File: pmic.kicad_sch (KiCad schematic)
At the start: 4 parts, among them U4 TPS6521907RHBR

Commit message: PMIC draft
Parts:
- added C25, C26, C27: GRM188R60J476ME15D, pepy_sym_lib:[CAP_SMD_0603_1608Metric], symbol pepy_sym_lib:[CAP_SMD_0603_1608Metric]Murata Electronics GRM188R60J476ME15D
- added C28, C29, C30, C31, C32, C33, C34, C35, C36: CC0402KRX5R6BB225, pepy_sym_lib:[CAP_SMD_0402_1005Metric], symbol pepy_sym_lib:[CAP_SMD_0402_1005Metric]YAGEO CC0402KRX5R6BB225
- added L3: FPA252012D-R33MT0, pepy_sym_lib:[P_IND_SMD_1008_2520Metric], symbol pepy_sym_lib:[P_IND_SMD_1008_2520Metric]cjiang (Changjiang Microelectronics Tec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
- added L4, L5: FTM252010CR47MCTA, pepy_sym_lib:[P_IND_SMD_1008_2520Metric], symbol pepy_sym_lib:[P_IND_SMD_1008_2520Metric]cjiang (Changjiang Microelectronics Tec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
- added R66, R67: 0402WGF0000TCE, pepy_sym_lib:[RES_SMD_0402_1005Metric], symbol pepy_sym_lib:[RES_SMD_0402_1005Metric]UNI-ROYAL(Uniroyal Elec) 0402WGF0000TCE
- added R68, R69, R70, R71, R72, R73: 0201WMF1002TEE, pepy_sym_lib:[RES_SMD_0201_0603Metric], symbol pepy_sym_lib:[RES_SMD_0201_0603Metric]UNI-ROYAL(Uniroyal Elec) 0201WMF1002TEE
- added TP10: VDDA_0V85, pepy_sym_lib:[TEST_POINT]TestPoint_Pad_D1.0mm, symbol pepy_sym_lib:[TEST_POINT]TestPoint
- added TP11: VDDA_1V8, 2, symbol pepy_sym_lib:[TEST_POINT]TestPoint
- added TP12: VDD_2V5, pepy_sym_lib:[TEST_POINT]TestPoint_Pad_D1.0mm, symbol pepy_sym_lib:[TEST_POINT]TestPoint
- added TP6: VDD_CORE, pepy_sym_lib:[TEST_POINT]TestPoint_Pad_D1.0mm, symbol pepy_sym_lib:[TEST_POINT]TestPoint
- added TP7: VDD_1V8, pepy_sym_lib:[TEST_POINT]TestPoint_Pad_D1.0mm, symbol pepy_sym_lib:[TEST_POINT]TestPoint
- added TP8: VDD_1V2, pepy_sym_lib:[TEST_POINT]TestPoint_Pad_D1.0mm, symbol pepy_sym_lib:[TEST_POINT]TestPoint
- added TP9: VDD_SD, pepy_sym_lib:[TEST_POINT]TestPoint_Pad_D1.0mm, symbol pepy_sym_lib:[TEST_POINT]TestPoint
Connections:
- net GND: now also C14.1, U4.15 (AGND), U4.33 (ThermalPad), C25.1, C26.1, C27.1, C28.2, C29.2, C30.2, C31.2, C32.2, C33.2, C34.2, C35.2, C36.2, R66.2, R70.1
- net VSYS_5V: now also U4.13 (VSYS), C32.1, R68.2
- net at U4.1 (FB_B1): now also R66.1, R67.1
- net I2C0_SCL: now reaches U4.10 (SCL)
- net EXTINTn: now reaches U4.11 (nINT)
- net EXTINTn: now also R72.1
- net SD_VOLT_SEL: now reaches U4.12 (VSEL_SD/VSEL_DDR)
- net SD_VOLT_SEL: now also R69.1, R70.2
- net at U4.14 (VDD1P8): now also C31.1
- net VDD_3V3_EN: now reaches U4.17 (GPO2)
- net MCU_PORz: now reaches U4.18 (nRSTOUT)
- net MCU_PORz: now also R73.1
- net VDDA_0V85: now reaches U4.19 (VLDO2)
- net VDDA_0V85: now also C34.1, TP10.1
- net at U4.2 (LX_B1_1): now also U4.3 (LX_B1_2), L3.2
- net VDD_1V8: now reaches U4.20 (PVIN_LDO2)
- net VDD_1V8: now also U4.32 (FB_B2), C26.2, C29.1, L4.1, TP7.1
- net VDDA_1V8: now reaches U4.21 (VLDO3)
- net VDDA_1V8: now also C35.1, TP11.1
- net VDD_3V3: now reaches U4.22 (PVIN_LDO34)
- net VDD_3V3: now also U4.6 (PVIN_LDO1), C28.1, C30.1, R69.2, R71.2, R72.2, R73.2
- net VDD_2V5: now reaches U4.23 (VLDO4)
- net VDD_2V5: now also C36.1, TP12.1
- net VDD_1V2: now reaches U4.24 (FB_B3)
- net VDD_1V2: now also C27.2, L5.1, TP8.1
- net PWR_BTN: now reaches U4.25 (EN/PB/VSENSE)
- net PWR_BTN: now also R68.1
- net at U4.27 (LX_B3): now also L5.2
- net RESETSTATz: now reaches U4.28 (MODE/RESET)
- net at U4.29 (LX_B2): now also L4.2
- net PMIC_LPM_EN0: now reaches U4.31 (MODE/STBY)
- net PMIC_LPM_EN0: now also R71.1
- net VDD_SD: now reaches U4.7 (VLDO1)
- net VDD_SD: now also C33.1, TP9.1
- net I2C0_SDA: now reaches U4.9 (SDA)
- new net VDD_CORE: C25.2, L3.1, R67.2, TP6.1
- no-connect marks 0 -> 2
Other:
- note added: "0.75V 3.5A"
- note added: "1.2V 2A"
- note added: "1.8V 0.4A"
- note added: "1.8V 2A"
- note added: "BUCK1_VSET [hexadecimal]: 0x06"
- note added: "BUCK2_VSET [hexadecimal]: 0x24"
- note added: "BUCK3_VSET [hexadecimal]: 0x18"
- note added: "Design: CSTB252012H-R33M ((1008[M:2520]), 6.9A, 330nH)"
- note added: "Design: CSTB252012H-R47M (1008[M:2520]), 5A, 470nH)"
- note added: "External 3V3 (and 1V8) DC gives the input power for the LDOs"
- note added: "External INT into SoC respective pin (pull-up to negated logic)"
- note added: "For any other purposes?"
- note added: "Internal Reference Voltage: For Internal Use Only. Bypass this pin to ground with a 2.2µF or greater ceramic capacitor."
- note added: "Main Domain warm reset status output"
- note added: "Power Input for BUCK1. Bypass this pin to ground with a 4.7μF or greater ceramic capacitor. Voltage on PVIN_B1_1 pin must not exceed voltage on VSYS pin."
- note added: "Since the power management is handled by the PMIC, it's reasonable to toggle it."
- note added: "The TPS65219 provides three step-down converters, four LDOs, three general-purpose I/Os and three multiFunction pins. The system can be supplied by a single cell Li-Ion battery, two primary cells or a regulated supply. The device is characterized across a -40°C to +105°C temperature range, which makes the PMIC an excellent choice for various industrial applications. The I2C interface provides com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"
- moved on the sheet: C19, U4

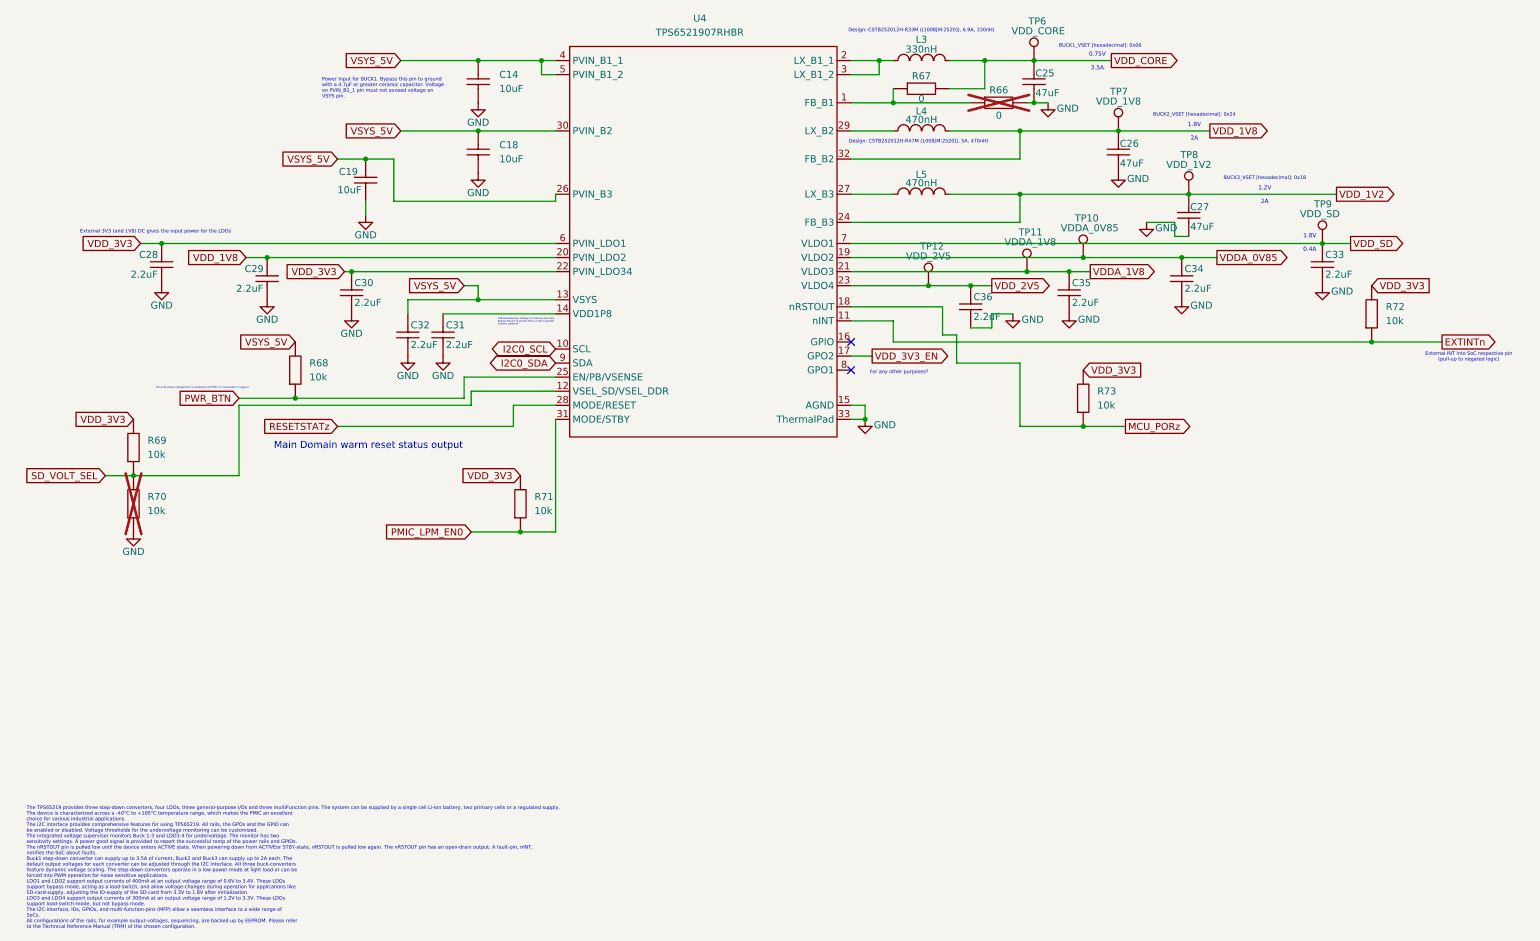
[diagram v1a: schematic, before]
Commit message: SD card changes
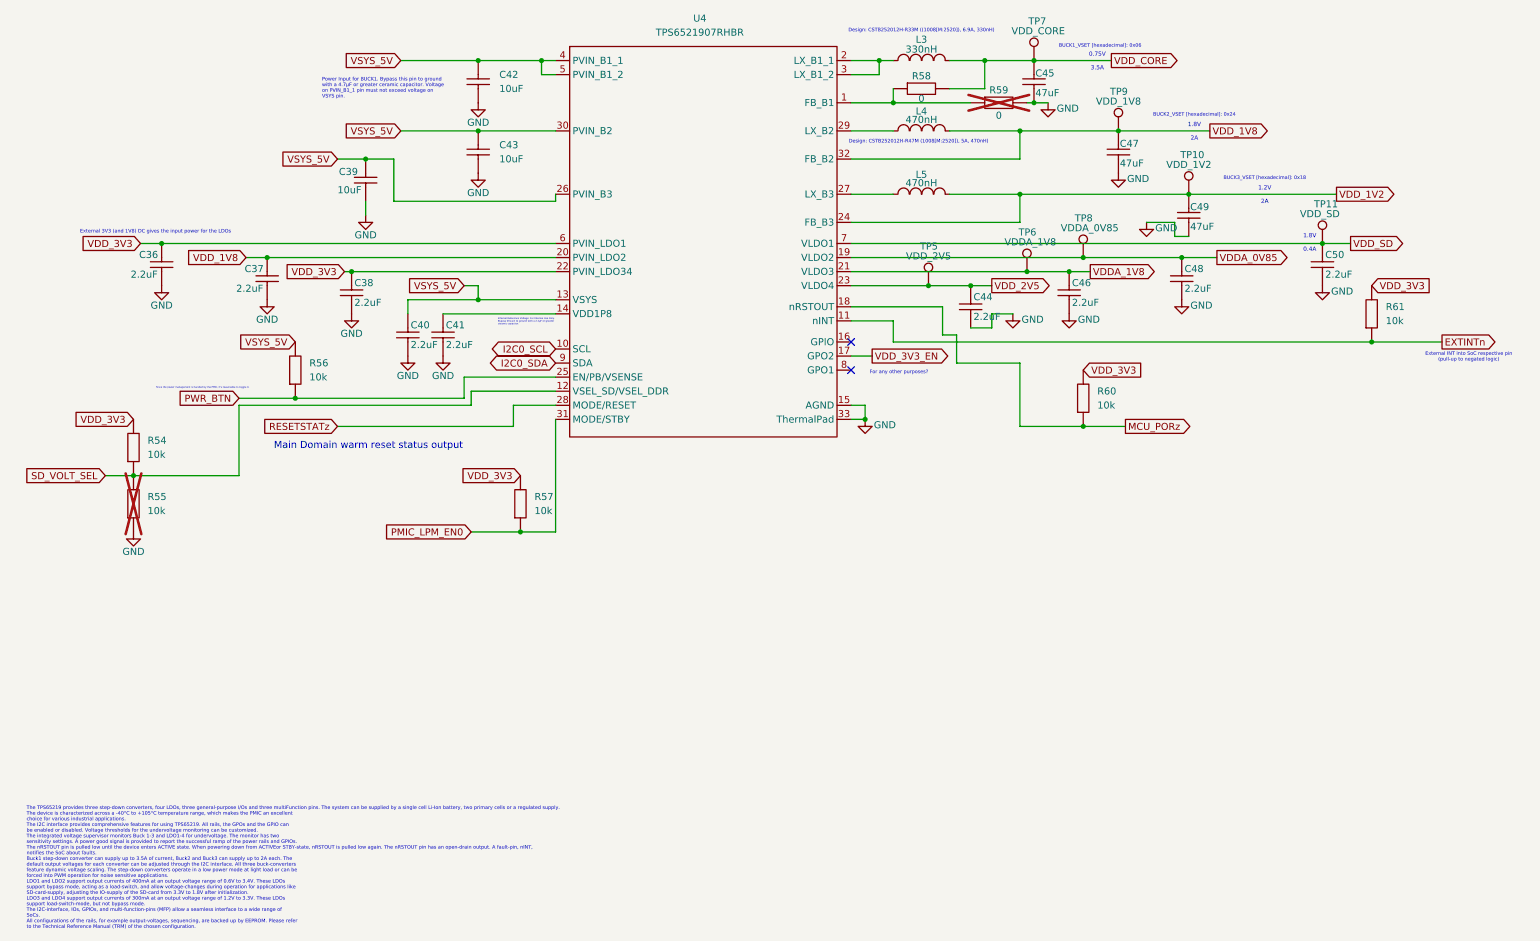
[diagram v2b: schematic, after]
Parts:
- renumbered C28 to C36, C29 to C37, C30 to C38, C19 to C39, C32 to C40, C31 to C41, C14 to C42, C18 to C43, C36 to C44, C25 to C45, C35 to C46, C26 to C47, C34 to C48, C27 to C49, C33 to C50, R69 to R54, R70 to R55, R68 to R56, R71 to R57, R67 to R58, R66 to R59, R73 to R60, R72 to R61, TP8 to TP10, TP9 to TP11, TP12 to TP5, TP11 to TP6, TP6 to TP7, TP10 to TP8, TP7 to TP9

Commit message: Bulk change
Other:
- note added: "1.8V/3.3V 0.4A"
- note removed: "1.8V 0.4A"
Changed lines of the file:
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@@
 		)
 	)
-	(text "1.8V\n\n0.4A"
+	(text "1.8V/3.3V\n\n\n0.4A"
 		(exclude_from_sim no)
-		(at 245.364 71.12 0)
+		(at 243.332 71.12 0)
 		(effects
 			(font
@@
 			"AAAAAIA/ZVUAAAAAAAAAAAAAAAAAAAAAAABwJetrqX8AAIhN+vhlVQAAAAAAAAAAAAAAAAAAAAAA"
 			"AIBN+vhlVQAAAAAAAAAAAAAAAAAAAAAAAJDMOe5lVQAACAAAAAAAAAAIAAAAAAAAAAIAAAAAAQAA"
-			"AAAAAAAAAAAAAAAAAAAAAMBhxvZlVQAACAAAAAAAAAAIAAAAAAAAAAAAAAAAAAAAAAAAAAAAAA=="
-		)
-	)
+			"AAAAAAAAAAAAAAAAAAAAAMBhxvZlVQAACAAAAAAAAAAIAAAAAAAAAAAAAAAAAAAAAAAAAAAAAAAA"
+			"AAAAAAAAAAAAAAAAAAAAAAAAAAAAAAAAAAAAAAAAAAAAAAAAAAAAAAAAAAAAAAAAAAAAAAAAAAAA"
+			"AAAAAAAAAAAAAAAAAAAAAAAAAAAAAAAAAAAAAAAAAAAAAAAAAAAAAAAAAAAAAAAAAAAAAAAAAAAA"
+			"AAAAAAAAAAAAAAAAAAAAAAAAAAAAAAAAAAAAAAAAAAAAAAAAAAAAAAAAAAAAAAAAAAAAAAAAAAAA"
+			"AAAAAAAAAAAAAAAAAAAAAAAAAAAAAAAAAAAAAAAAAAAAAAAAAAAAAAAAAAAAAAAAAAAAAAAAAAAA"
+			"AAAAAAAAAAAAAAAAAAAAAAAAAAAAAAAAAAAAAAAAAAAAAAAAAAAAAAAAAAAAAAAAAAAAAAAAAAAA"
+			"AAAAAAAAAAAAAAAAAAAAAAAAAAAAAAAAAAAAAAAAAAAAAAAAAAAAAAAAAAAAAAAAAAAAAAAAAAAA"
+			"AAAAAAAAAAAAAAAAAAAAAAAAAAAAAAAAAAAAAAAAAAAAAAAAAAAAAAAAAAAAAAAAAAAAAAAAAAAA"
+			"AAAAAAAAAAAAAAAAAAAAAAAAAAAAAAAAAAAAAAAAAAAAAAAAAAAAAAAAAAAAAAAAAAAAAAAAAAAA"
+			"AAAAAAAAAAAAAAAAAAAAAAAAAAAAAAAAAAAAAAAAAAAAAAAAAAAAAAAAAAAAAAAAAAAAAAAAAAAA"
+			"AAAAAAAAAAAAAAAAAAAAAAAAAAAAAAAAAAAAAAAAAAAAAAAAAAAAAAAAAAAAAAAAAAAAAAAAAAAA"
+			"AAAAAAAAAAAAAAAAAAAAAAAAAAAAAAAAAAAAAAAAAAAAAAAAAAAAAAAAAAAAAAAAAAAAAAAAAAAA"
+			"AAAAAAAAAAAAAAAAAAAAAAAAAAAAAAAAAAAAAAAAAAAAAAAAAAAAAAAAAAAAAAAAAAAAAAAAAAAA"
+			"AAAAAAAAAAAAAAAAAAAAAAAAAAAAAAAAAAAAAAAAAAAAAAAAAAAAAAAAAAAAAAAAAAAAAAAAAAAA"
+			"AAAAAAAAAAAAAAAAAAAAAAAAAAAAAAAAAAAAAAAAAAAAAAAAAAAAAAAAAAAAAAAAAAAAAAAAAAAA"
+			"AAAAAAAAAAAAAAAAAAAAAAAAAAAAAAAAAAAAAAAAAAAAAAAAAAAAAAAAAAAAAAAAAAAAAAAAAAAA"
+			"AAAAAAAAAAAAAAAAAAAAAAAAAAAAAAAAAAAAAAAAAAAAAAAAAAAAAAAAAAAAAAAAAAAAAAAAAAAA"
+			"AAAAAAAAAAAAAAAAAAAAAAAAAAAAAAAAAAAAAAAAAAAAAAAAAAAAAAAAAAAAAAAAAAAAAAAAAAAA"
+			"AAAAAAAAAAAAAAAAAAAAAAAAAAAAAAAAAAAAAAAAAAAAAAAAAAAAAAAAAAAAAAAAAAAAAAAAAA=="
+		)
+	)
